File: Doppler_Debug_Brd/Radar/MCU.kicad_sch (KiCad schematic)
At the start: 31 parts, among them J1 AVR-PDI-6, J2 USB_B, U1 LM3671MF-3.3/NOPB, U2 ATxmega256A3U-A, U3 FT231XS

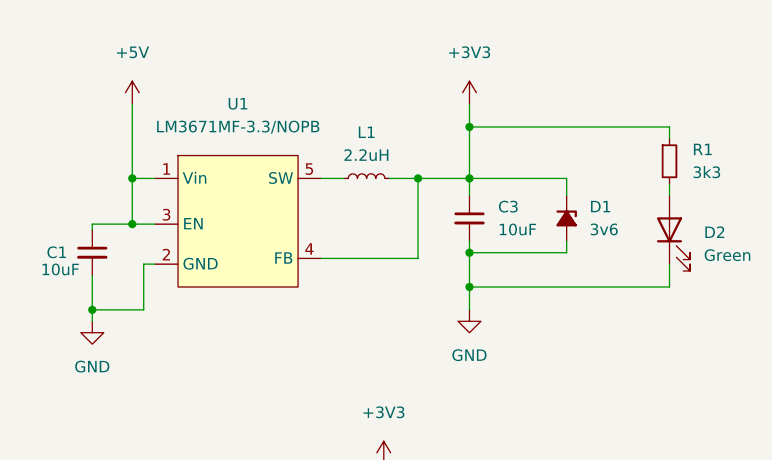
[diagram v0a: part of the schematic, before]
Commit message: fixed stability output plus raw sample debugging
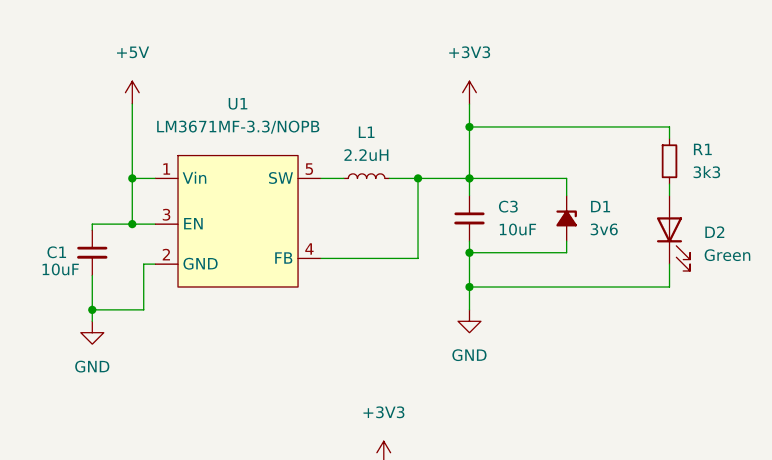
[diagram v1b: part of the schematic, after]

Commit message: Finalized code
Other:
- title: (none) -> Doppler Debug Board (Digital)
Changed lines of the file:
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@@
 (kicad_sch (version 20230121) (generator eeschema)
   (paper "A4")
+  (title_block
+    (title "Doppler Debug Board (Digital)")
+    (date "2023-09-18")
+    (rev "AB")
+  )
   (junction (at 64.135 71.12) (diameter 0) (color 0 0 0 0)
   )
